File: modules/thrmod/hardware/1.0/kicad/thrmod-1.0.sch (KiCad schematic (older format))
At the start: 45 parts, among them J1 Screw_Terminal_01x02, J2 Screw_Terminal_01x02, J3 SWITCHES, J4 CAN, K1 FINDER-32.21-x300, K2 FINDER-32.21-x300, Q1 NTE123A, Q2 NTE123A, SW1 SCR, SW2 MODE, SW3 INSTANCE, U1 PDJR_Teensy_3.2, U2 MCP2551-I-P, U3 TMR-1-1211, U4 CNY74-2H

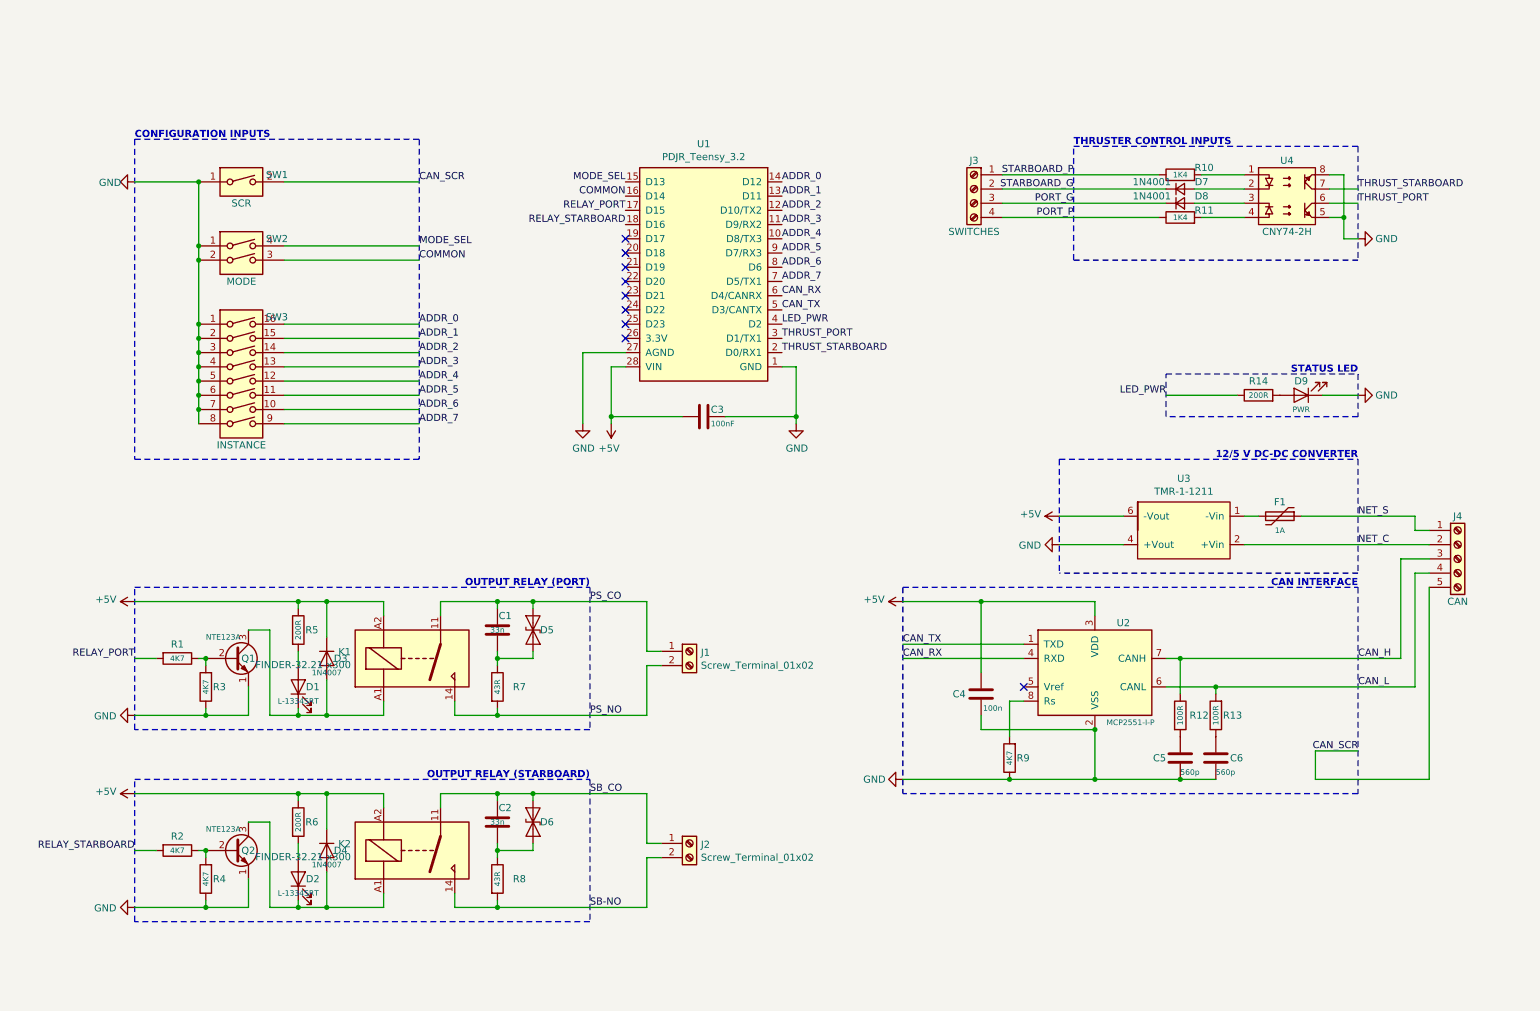
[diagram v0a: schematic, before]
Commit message: Add thruster firmware
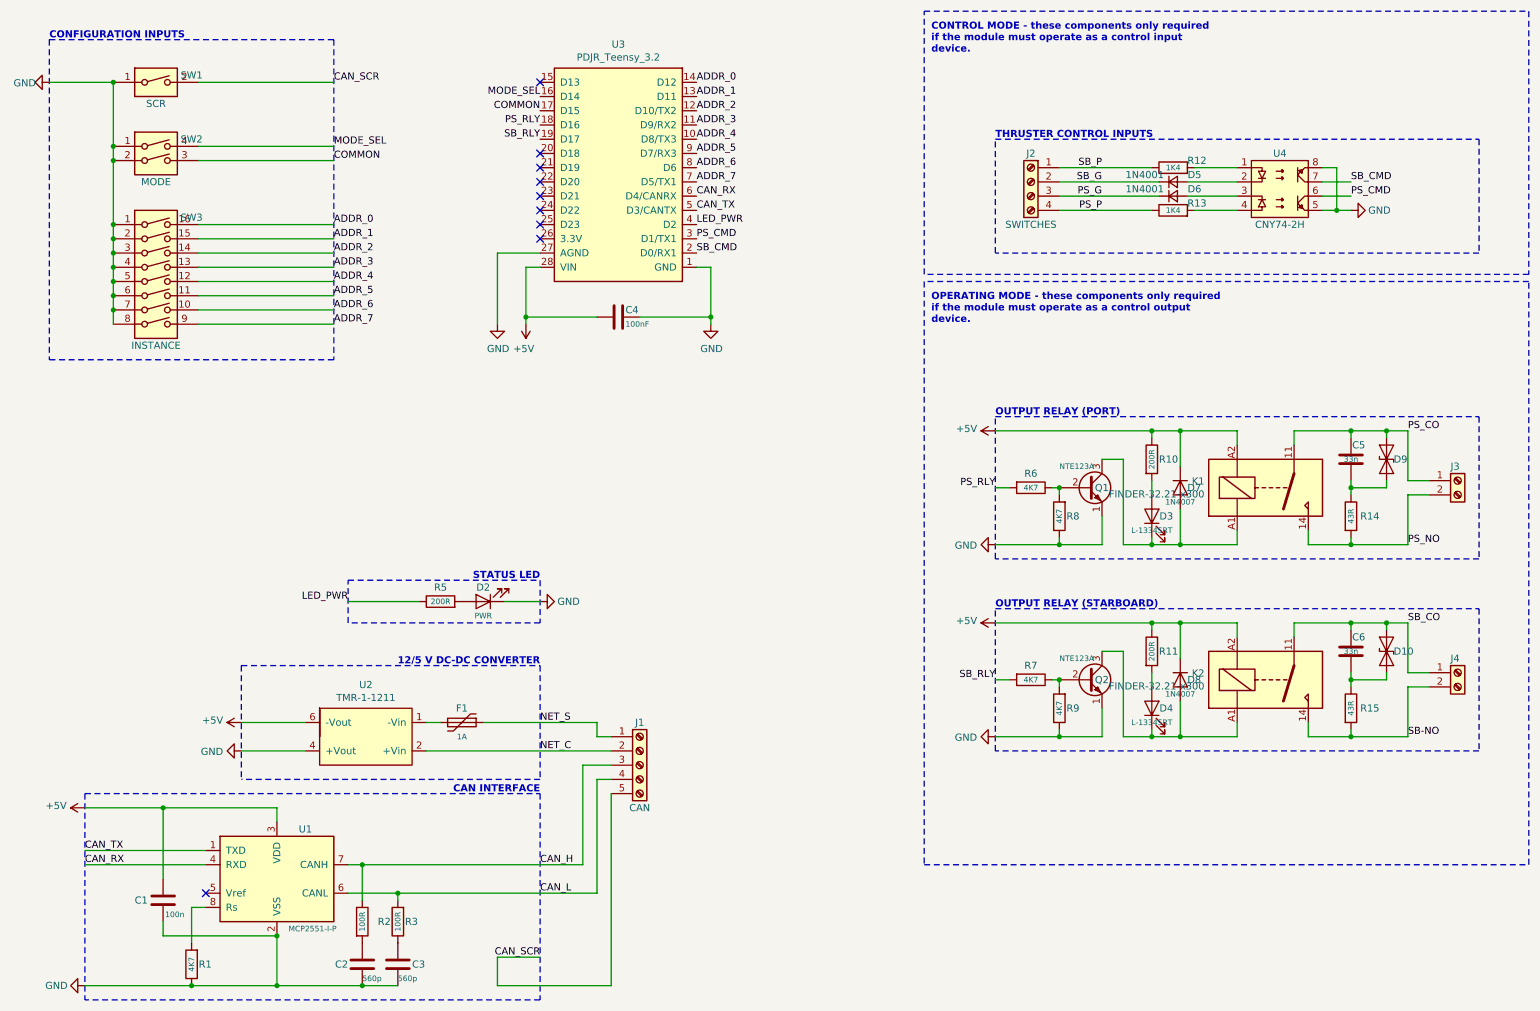
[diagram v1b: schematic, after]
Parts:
- renumbered C4 to C1, C5 to C2, C6 to C3, C3 to C4, C1 to C5, C2 to C6, D6 to D10, D9 to D2, D1 to D3, D2 to D4, D7 to D5, D8 to D6, D3 to D7, D4 to D8, D5 to D9, J4 to J1, J3 to J2, J1 to J3, J2 to J4, R9 to R1, R5 to R10, R6 to R11, R10 to R12, R11 to R13, R7 to R14, R8 to R15, R12 to R2, R13 to R3, R14 to R5, R1 to R6, R2 to R7, R3 to R8, R4 to R9, U2 to U1, U3 to U2, U1 to U3
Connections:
- net COMMON: now also U3.17 (D15); no longer U3.16 (D14)
- net MODE_SEL: now also U3.16 (D14); no longer U3.15 (D13)
- net SB_RLY: now reaches U3.19 (D17)
- net SB_RLY: now also R7.2
- net PORT_G renamed PS_G
- net PORT_P renamed PS_P
- net RELAY_PORT renamed PS_RLY
- net PS_RLY: now also U3.18 (D16); no longer U3.17 (D15)
- removed net RELAY_STARBOARD: R7.2, U3.18 (D16)
- net STARBOARD_G renamed SB_G
- net STARBOARD_P renamed SB_P
- net THRUST_PORT renamed PS_CMD
- net THRUST_STARBOARD renamed SB_CMD
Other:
- note added: "CONTROL MODE - these components only required\nif the module must operate as a control input\ndevice."
- note added: "OPERATING MODE - these components only required\nif the module must operate as a control output\ndevice."
- moved on the sheet: C1, C2, C3, C4, C5, C6, D10, D2, D3, D4, D5, D6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
